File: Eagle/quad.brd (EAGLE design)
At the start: 100 x 60 mm, 15 parts

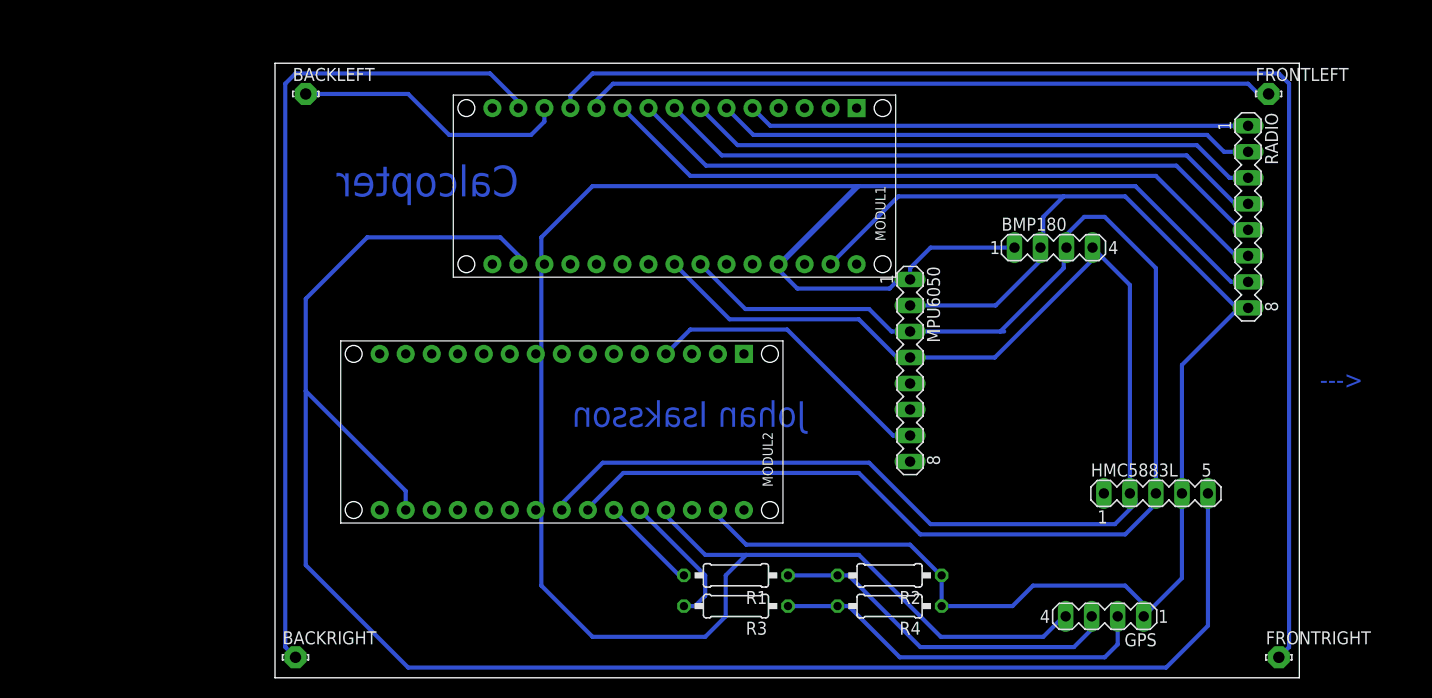
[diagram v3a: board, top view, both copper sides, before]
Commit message: Fixed trace width.
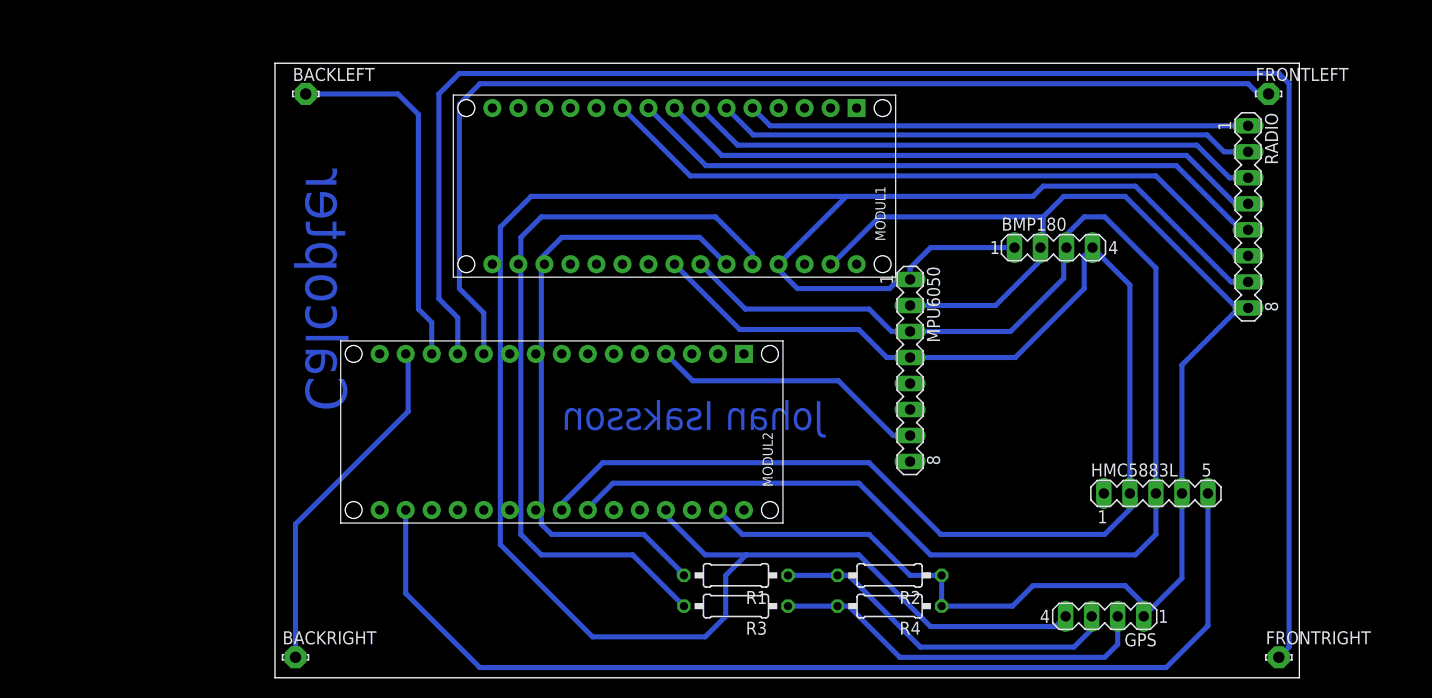
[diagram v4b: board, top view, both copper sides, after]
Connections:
- new net COM: MODUL1.J1.4
- new net N$10: MODUL1.J2.6, R1.2
- net N$1: now also MODUL2.J1.11; no longer MODUL1.J1.11
- net N$14: no longer MODUL1.J2.14
- net N$15: now also MODUL1.J2.14; no longer MODUL2.J2.5, R3.2
- net N$18: now also MODUL1.J2.5, R3.2; no longer MODUL2.J2.6, R1.2
- net N$3: now also MODUL2.J1.13; no longer MODUL1.J1.13
- net N$4: now also MODUL2.J1.14; no longer MODUL1.J1.14
- net N$6: now also MODUL2.J1.12; no longer MODUL1.J1.12
- net N$9: no longer MODUL1.J1.4
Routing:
- net N$14: track 173.5 -> 104.1 mm
- net N$18: track 9.48 -> 73.8 mm
- net N$10: track 0.00 -> 61.8 mm
- net N$4: track 81.6 -> 34.4 mm
- net N$1: track 67.8 -> 105.6 mm
- net N$6: track 129.1 -> 166.8 mm
- net N$15: track 13.5 -> 0.00 mm
- net N$3: track 26.8 -> 35.7 mm
- net N$2: track 231.0 -> 223.7 mm
- net N$9: track 184.5 -> 179.4 mm
- net N$16: track 139.9 -> 143.7 mm
- net N$17: track 138.2 -> 141.1 mm
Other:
- board text removed: "<---"

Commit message: Final board design and added ground fill.
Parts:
- removed BMP180: (no value), con-lstb:MA04-1
- moved GPS 74.5 mm to (12.0, 34.0), turned to 0 degrees
- moved R4 64.4 mm to (13.0, 51.0), turned to 0 degrees
- moved R2 59.8 mm to (13.0, 47.0), turned to 0 degrees
- moved R3 47.5 mm to (27.0, 51.0), turned to 0 degrees
- moved R1 41.1 mm to (27.0, 47.0), turned to 0 degrees
- moved MODUL2 9.22 mm to (35.0, 18.0)
- moved RADIO 5.39 mm to (90.0, 47.0)
- moved FRONTLEFT 5.00 mm to (94.0, 61.0)
- moved MODUL1 4.47 mm to (35.0, 50.0)
- moved BACKLEFT 4.12 mm to (4.00, 61.0)
- moved FRONTRIGHT 4.12 mm to (94.0, 3.00)
- moved MPU6050 2.83 mm to (60.0, 32.0)
- moved BACKRIGHT 2.24 mm to (4.00, 3.00)
- moved HMC5883L 2.00 mm to (84.0, 18.0)
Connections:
- removed net COM: MODUL1.J1.4
- removed net N$2: BMP180.1, GPS.4, MODUL1.J2.4, MODUL2.J2.4, MPU6050.1, RADIO.7
- removed net N$9: BMP180.2, GPS.1, HMC5883L.4, MODUL1.J2.2, MODUL2.J1.4, MODUL2.J2.2, MPU6050.2, MPU6050.7, R2.1, R4.1, RADIO.8
- new net GND: GPS.1, HMC5883L.4, MODUL1.J1.4, MODUL1.J2.2, MODUL2.J1.4, MODUL2.J2.2, MPU6050.2, MPU6050.7, R2.1, R4.1, RADIO.8
- new net VDD: GPS.4, MODUL1.J2.4, MODUL2.J2.4, MPU6050.1, RADIO.7
- net N$16: no longer BMP180.3
- net N$17: no longer BMP180.4
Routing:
- net VDD: track 0.00 -> 276.9 mm
- net N$2: track 223.7 -> 0.00 mm
- net GND: track 0.00 -> 185.8 mm
- net N$9: track 179.4 -> 0.00 mm
- net N$6: track 166.8 -> 106.8 mm
- net N$18: track 73.8 -> 14.1 mm
- net N$10: track 61.8 -> 10.2 mm
- net N$1: track 105.6 -> 155.1 mm
- net N$14: track 104.1 -> 72.1 mm
- net N$16: track 143.7 -> 116.8 mm
- net N$17: track 141.1 -> 114.5 mm
- net N$3: track 35.7 -> 52.0 mm
- net N$20: track 34.5 -> 20.6 mm
- net N$21: track 37.5 -> 26.9 mm
- net N$4: track 34.4 -> 29.3 mm
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- added copper zone on layer 16, net GND
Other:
- board size 100 x 60 mm -> 98 x 64 mm
